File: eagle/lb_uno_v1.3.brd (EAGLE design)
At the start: 68.6 x 53.3 mm, 16 parts, among them SW1 Button, SW3 Encoder

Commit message: updated board designs and docs
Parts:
- PCB1: value ARDUINO_UNO -> ARDUINO_UNO_V2; device E14_Arduino_revC:ARDUINO_UNO -> E14_Arduino_revC:ARDUINO_UNO_V2
- R1: value 330 -> 10k
- R4: value 10k -> 330
- SW3: value Encoder -> Rotary Encoder
- moved R4 22.9 mm to (-49.5, 36.8)
- moved R1 8.89 mm to (-49.5, 14.0), turned to 180 degrees
- moved R2 7.62 mm to (-49.5, 22.9), turned to 0 degrees
- moved R3 6.35 mm to (-49.5, 30.5)
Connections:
- net D10: now also R4.1; no longer R3.1
- net D7: now also R1.2; no longer R4.2
- net D8: now also R2.2; no longer R1.2
- net D9: now also R3.1; no longer R2.1
- net GND: now also R1.1; no longer R4.1
- net N$1: now also R2.1; no longer R1.1
- net N$2: now also R3.2; no longer R2.2
- net N$3: now also R4.2; no longer R3.2
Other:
- outline, holes or cut-outs redrawn
- board text added: "+"
- board text added: "Made for Foundations of Fabrication at MakeHaven in New Haven, CT, USA"
- board text added: "Rotary encoder on digital pins 2 & 3, which are also interrupt pins (bonus feature). The encoder also has a button integrated in the shaft - on pin 4. Simple LED on pin 8 (not hardware PWM). The RGB led is on pins 9, 10, 11 (all PWM enabled) and colors probably in order: 9-red, 10-green, 11-blue. Button on pin 7. *All buttons are logic HIGH when pressed. Potentiomer (pot) on pin A0. Photoresistor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"
- board text added: "Soldering: Inputs and Outputs"
- board text added: "V1.3 Deigned by Corey Rice 7/2020"
- board text added: "https://github.com/crice009/Arduino_Learning_Board"

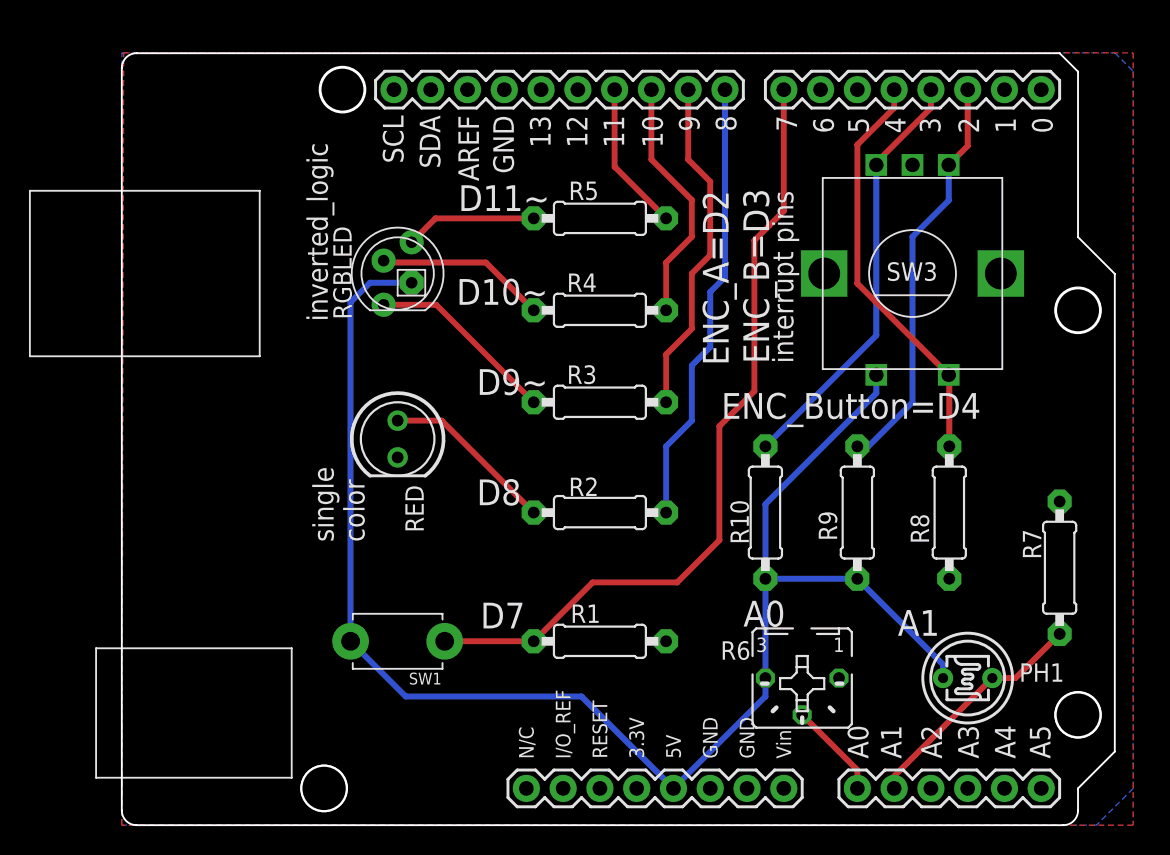
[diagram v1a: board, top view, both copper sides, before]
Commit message: added 555 circuit
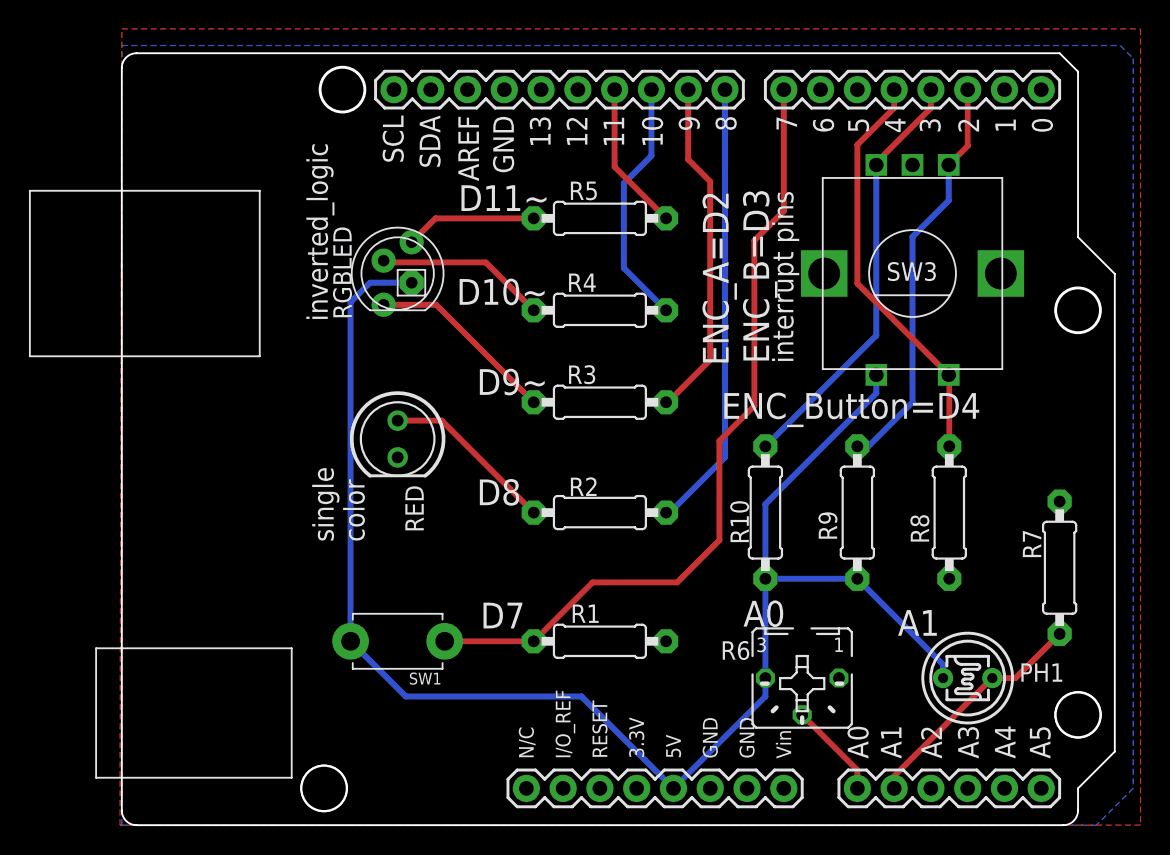
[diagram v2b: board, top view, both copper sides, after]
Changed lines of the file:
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@@
 <grid distance="5" unitdist="mil" unit="mil" style="lines" multiple="1" display="no" altdistance="5" altunitdist="mil" altunit="mil"/>
 <layers>
-<layer number="1" name="Top" color="4" fill="1" visible="no" active="yes"/>
+<layer number="1" name="Top" color="4" fill="1" visible="yes" active="yes"/>
 <layer number="2" name="Route2" color="16" fill="1" visible="no" active="no"/>
 <layer number="3" name="Route3" color="17" fill="1" visible="no" active="no"/>
@@
 <layer number="14" name="Route14" color="22" fill="1" visible="no" active="no"/>
 <layer number="15" name="Route15" color="23" fill="1" visible="no" active="no"/>
-<layer number="16" name="Bottom" color="1" fill="1" visible="no" active="yes"/>
+<layer number="16" name="Bottom" color="1" fill="1" visible="yes" active="yes"/>
 <layer number="17" name="Pads" color="2" fill="1" visible="yes" active="yes"/>
 <layer number="18" name="Vias" color="2" fill="1" visible="yes" active="yes"/>
@@
 <contactref element="RED" pad="OUT"/>
 <polygon width="0.4064" layer="16">
-<vertex x="-82.55" y="54.61"/>
-<vertex x="-13.97" y="54.61"/>
-<vertex x="-12.7" y="53.34"/>
+<vertex x="-82.55" y="55.118"/>
+<vertex x="-13.589" y="55.118"/>
+<vertex x="-12.7" y="54.229"/>
 <vertex x="-12.7" y="3.81"/>
 <vertex x="-15.24" y="1.27"/>
@@
 </polygon>
 <polygon width="0.4064" layer="1">
-<vertex x="-82.423" y="54.61"/>
-<vertex x="-12.7" y="54.61"/>
-<vertex x="-12.7" y="1.27"/>
-<vertex x="-82.55" y="1.27"/>
+<vertex x="-82.54606875" y="56.261"/>
+<vertex x="-12.192" y="56.261"/>
+<vertex x="-12.192" y="1.27"/>
+<vertex x="-82.677" y="1.27"/>
 </polygon>
-<wire x1="-44.958" y1="13.97" x2="-41.91" y2="3.81" width="0" layer="19" extent="1-1"/>
-<wire x1="-33.02" y1="11.43" x2="-41.91" y2="3.81" width="0" layer="19" extent="1-1"/>
-<wire x1="-25.4" y1="18.288" x2="-33.02" y2="11.43" width="0" layer="19" extent="1-1"/>
-<wire x1="-17.78" y1="23.622" x2="-25.4" y2="18.288" width="0" layer="19" extent="1-1"/>
-<wire x1="-63.5" y1="26.67" x2="-44.958" y2="13.97" width="0" layer="19" extent="1-1"/>
-<wire x1="-27.94" y1="46.87" x2="-17.78" y2="23.622" width="0" layer="19" extent="1-1"/>
-<wire x1="-56.134" y1="52.07" x2="-63.5" y2="26.67" width="0" layer="19" extent="1-1"/>
 </signal>
 <signal name="D11">
@@
 <contactref element="PCB1" pad="10"/>
 <contactref element="R4" pad="1"/>
-<wire x1="-44.958" y1="36.83" x2="-44.958" y2="40.132" width="0.4064" layer="1"/>
-<wire x1="-43.18" y1="41.91" x2="-43.18" y2="44.45" width="0.4064" layer="1"/>
-<wire x1="-43.18" y1="44.45" x2="-45.974" y2="47.244" width="0.4064" layer="1"/>
-<wire x1="-45.974" y1="47.244" x2="-45.974" y2="52.07" width="0.4064" layer="1"/>
-<wire x1="-44.958" y1="40.132" x2="-43.18" y2="41.91" width="0.4064" layer="1"/>
+<wire x1="-45.974" y1="52.07" x2="-45.974" y2="47.498" width="0.4064" layer="16"/>
+<wire x1="-45.974" y1="47.498" x2="-47.879" y2="45.593" width="0.4064" layer="16"/>
+<wire x1="-47.879" y1="45.593" x2="-47.879" y2="39.751" width="0.4064" layer="16"/>
+<wire x1="-47.879" y1="39.751" x2="-44.958" y2="36.83" width="0.4064" layer="16"/>
 </signal>
 <signal name="D9">
 <contactref element="PCB1" pad="9"/>
 <contactref element="R3" pad="1"/>
-<wire x1="-44.958" y1="30.48" x2="-44.958" y2="33.782" width="0.4064" layer="1"/>
-<wire x1="-44.958" y1="33.782" x2="-43.18" y2="35.56" width="0.4064" layer="1"/>
-<wire x1="-43.18" y1="35.56" x2="-43.18" y2="39.37" width="0.4064" layer="1"/>
-<wire x1="-43.18" y1="39.37" x2="-41.91" y2="40.64" width="0.4064" layer="1"/>
-<wire x1="-41.91" y1="40.64" x2="-41.91" y2="45.72" width="0.4064" layer="1"/>
+<wire x1="-41.91" y1="33.401" x2="-44.831" y2="30.48" width="0.4064" layer="1"/>
+<wire x1="-44.958" y1="30.48" x2="-44.831" y2="30.48" width="0.4064" layer="1"/>
+<wire x1="-41.91" y1="33.401" x2="-41.91" y2="45.72" width="0.4064" layer="1"/>
 <wire x1="-43.434" y1="47.244" x2="-43.434" y2="52.07" width="0.4064" layer="1"/>
 <wire x1="-41.91" y1="45.72" x2="-43.434" y2="47.244" width="0.4064" layer="1"/>
@@
 <contactref element="PCB1" pad="8"/>
 <contactref element="R2" pad="2"/>
-<wire x1="-44.958" y1="22.86" x2="-44.958" y2="27.432" width="0.4064" layer="16"/>
-<wire x1="-43.18" y1="29.21" x2="-43.18" y2="33.02" width="0.4064" layer="16"/>
-<wire x1="-43.18" y1="33.02" x2="-41.91" y2="34.29" width="0.4064" layer="16"/>
-<wire x1="-41.91" y1="34.29" x2="-41.91" y2="38.1" width="0.4064" layer="16"/>
-<wire x1="-40.894" y1="39.116" x2="-40.894" y2="52.07" width="0.4064" layer="16"/>
-<wire x1="-44.958" y1="27.432" x2="-43.18" y2="29.21" width="0.4064" layer="16"/>
-<wire x1="-41.91" y1="38.1" x2="-40.894" y2="39.116" width="0.4064" layer="16"/>
+<wire x1="-40.894" y1="26.67" x2="-40.894" y2="52.07" width="0.4064" layer="16"/>
+<wire x1="-44.958" y1="22.86" x2="-44.704" y2="22.86" width="0.4064" layer="16"/>
+<wire x1="-40.894" y1="26.67" x2="-44.704" y2="22.86" width="0.4064" layer="16"/>
 </signal>
 <signal name="D7">
@@
 <wire x1="-50.038" y1="18.034" x2="-44.196" y2="18.034" width="0.4064" layer="1"/>
 <wire x1="-44.196" y1="18.034" x2="-41.275" y2="20.955" width="0.4064" layer="1"/>
-<wire x1="-41.275" y1="20.955" x2="-41.275" y2="28.829" width="0.4064" layer="1"/>
-<wire x1="-41.275" y1="28.829" x2="-38.862" y2="31.242" width="0.4064" layer="1"/>
-<wire x1="-38.862" y1="31.242" x2="-38.862" y2="41.656" width="0.4064" layer="1"/>
+<wire x1="-41.275" y1="20.955" x2="-41.275" y2="27.813" width="0.4064" layer="1"/>
+<wire x1="-41.275" y1="27.813" x2="-38.862" y2="30.226" width="0.4064" layer="1"/>
+<wire x1="-38.862" y1="30.226" x2="-38.862" y2="41.656" width="0.4064" layer="1"/>
 <wire x1="-38.862" y1="41.656" x2="-36.83" y2="43.688" width="0.4064" layer="1"/>
 <wire x1="-36.83" y1="43.688" x2="-36.83" y2="52.07" width="0.4064" layer="1"/>
